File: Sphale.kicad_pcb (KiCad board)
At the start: 2 copper layers, 17.8 x 33 mm, 29 parts, among them J1 USB_C_Receptacle_USB2.0, J2 Conn_01x12, J3 Conn_01x12, J4 Conn_01x05, SW1 RESET, SW3 BOOT, U1 STM32F303CCTx, U2 RT9013-33GB, Y1 8MHz

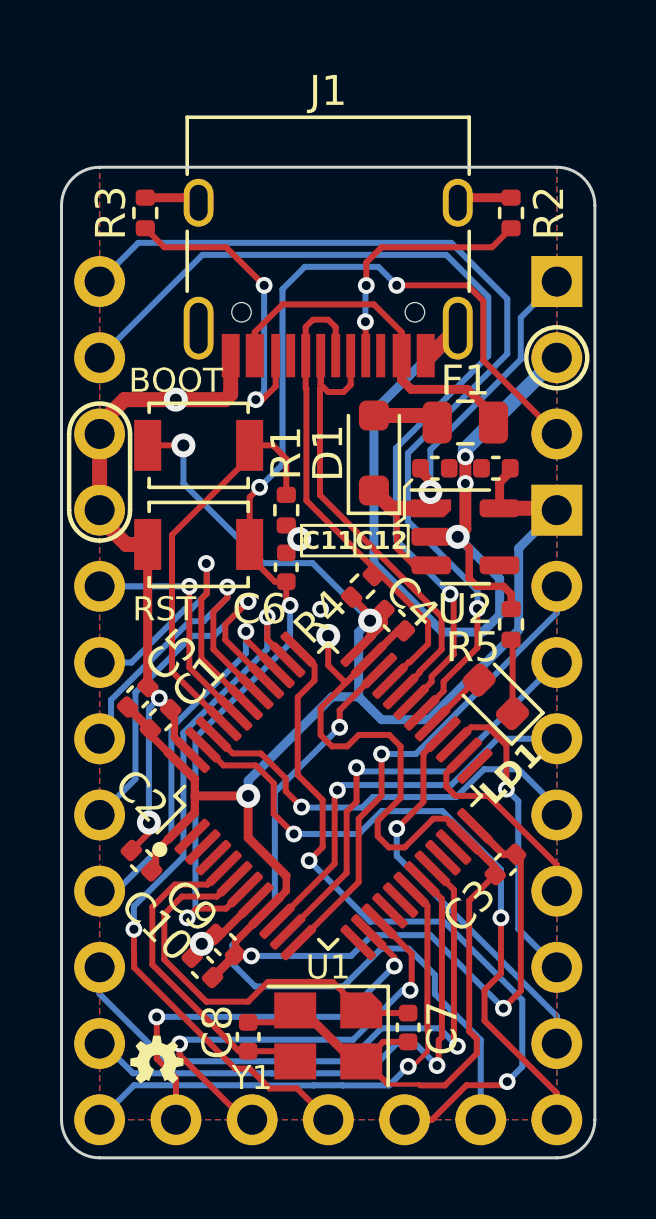
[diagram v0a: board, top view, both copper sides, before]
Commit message: Update BOM and references
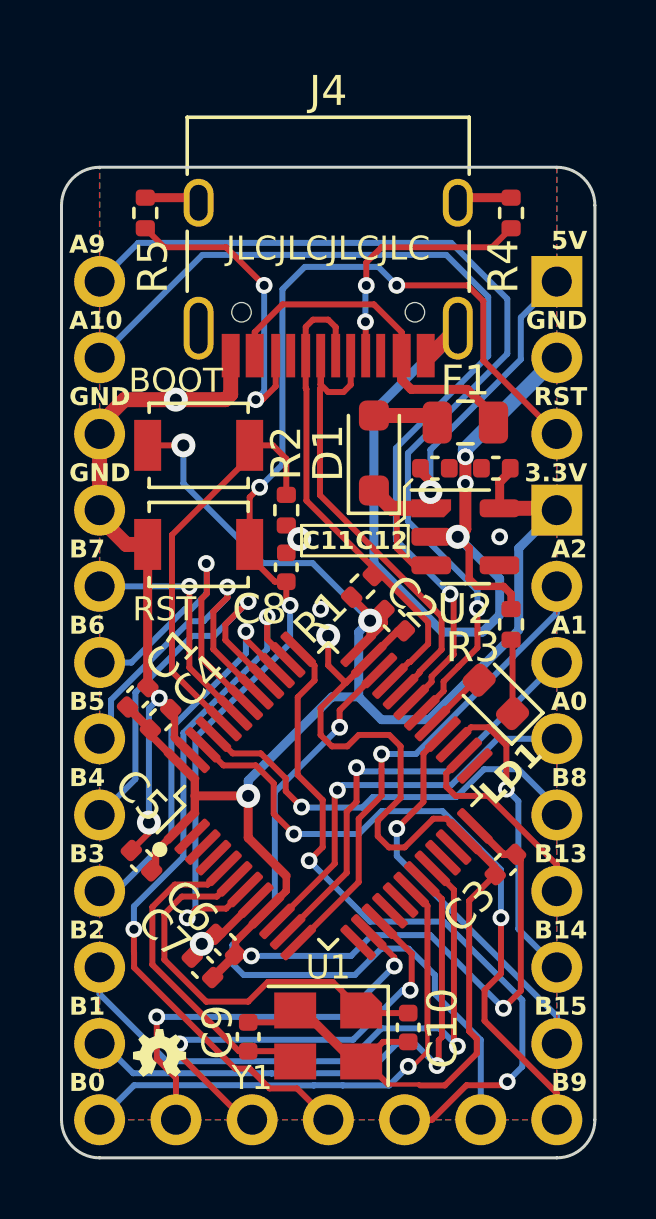
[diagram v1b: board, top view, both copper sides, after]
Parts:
- R3: renamed from R5; value 10k -> 5.1k
- renumbered C5 to C1, C7 to C10, C4 to C2, C1 to C4, C2 to C5, C9 to C6, C10 to C7, C6 to C8, C8 to C9, J2 to J1, J3 to J2, J4 to J3, J1 to J4, R4 to R1, R1 to R2, R2 to R4, R3 to R5, SW3 to SW2
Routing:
- net GND: vias 10 -> 11
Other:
- board text added: "JLCJLCJLCJLC"
